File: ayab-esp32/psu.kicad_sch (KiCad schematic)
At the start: 48 parts, among them U401 XL1509, U402 XL1509

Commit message: first draft schematic
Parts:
- removed C? (x4): 10uF, Capacitor_SMD:C_0603_1608Metric, symbol Device:C_Small
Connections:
- net +12V: no longer C?.1, C?.1, C?.1, C?.1, C?.1, C?.1, C?.1, D403.1 (K), J?.1, TP402.1
- net +3V3: no longer C419.2, C421.1, L402.2, R407.2
- net +5V: no longer C418.2, C420.1, L401.2, R406.2
- new net 12V: C?.1, C?.1, C?.1, C?.1, C?.1, C?.1, C?.1, D403.1 (K), J?.1, TP402.1
- new net 3V3: C419.2, C421.1, L402.2, R407.2
- new net 5V: C418.2, C420.1, L401.2, R406.2
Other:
- company: matei repair lab -> matei
- moved on the sheet: C?, D403, J?, TP401, TP402, TP403

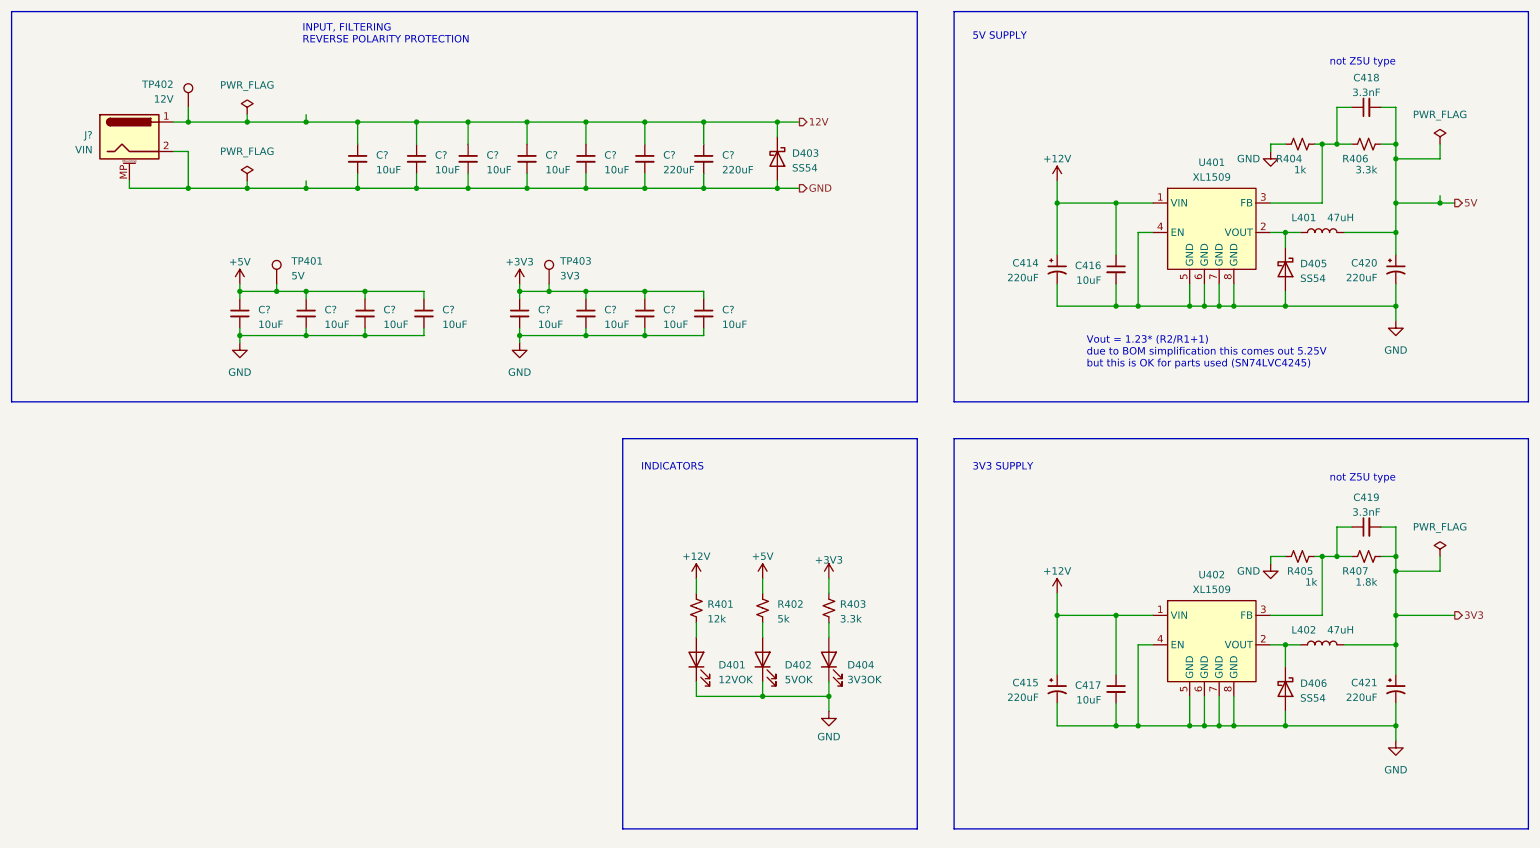
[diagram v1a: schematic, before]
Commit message: add pch MOSFET for polarity protection
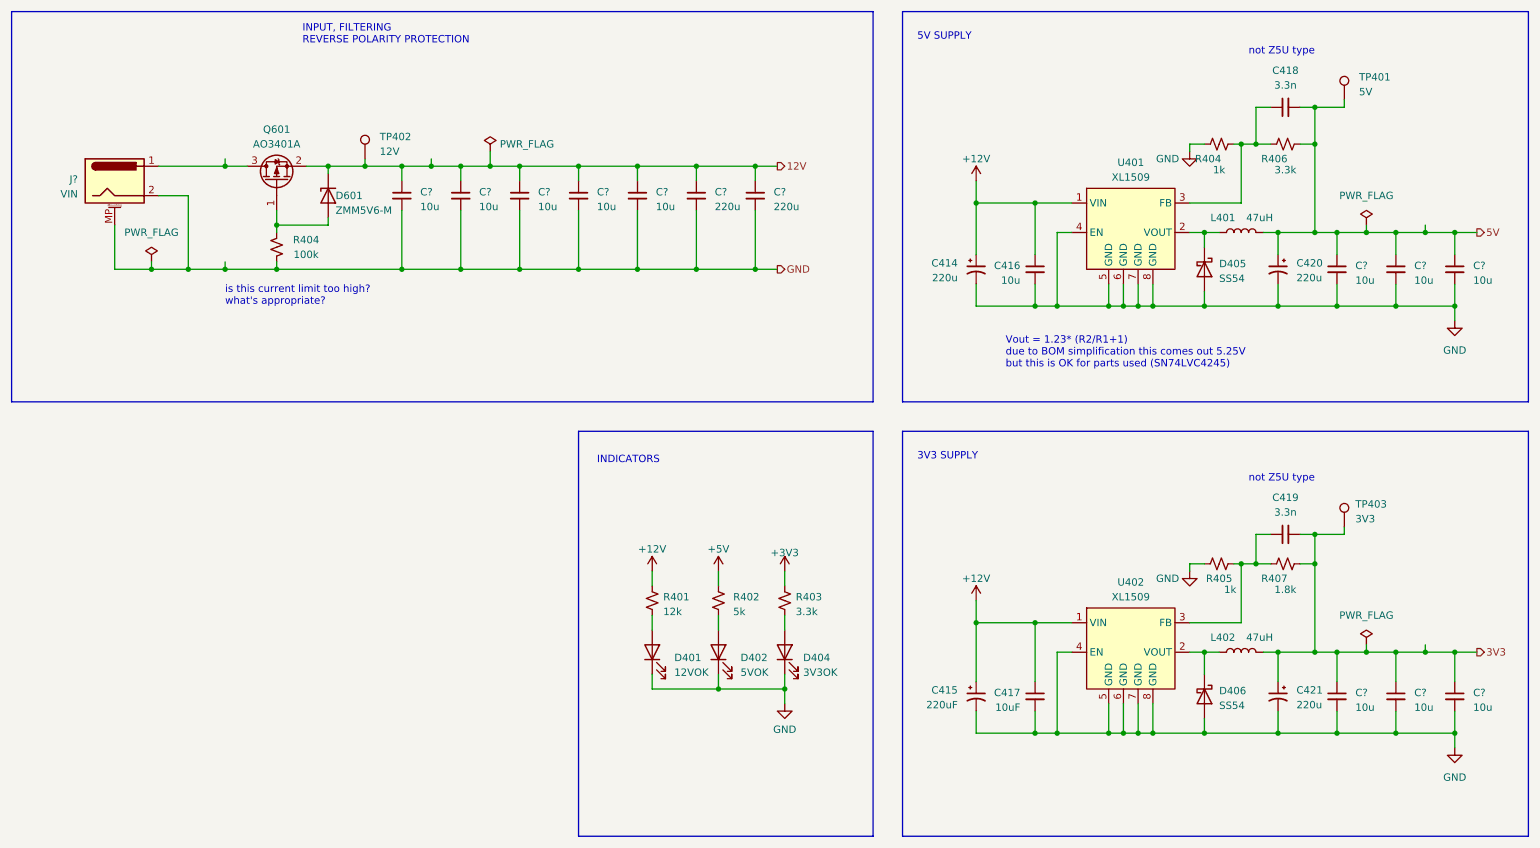
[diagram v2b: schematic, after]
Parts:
- removed C? (x2): 10uF, Capacitor_SMD:C_0603_1608Metric, symbol Device:C_Small
- removed D403: SS54, Diode_SMD:D_SMA, symbol Device:D_Schottky
- added D601: ZMM5V6-M, symbol Device:D_Zener
- added Q601: AO3401A, Package_TO_SOT_SMD:SOT-23, symbol Transistor_FET:AO3401A
- added R404: 100k, Resistor_SMD:R_0603_1608Metric, symbol Device:R_Small_US
- C414, C420, C421, C? (x2): value 220uF -> 220u
- C416, C? (x11): value 10uF -> 10u
- C418, C419: value 3.3nF -> 3.3n
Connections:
- net +3V3: no longer C?.1, C?.1, C?.1, TP403.1
- net +5V: no longer C?.1, C?.1, C?.1, TP401.1
- net 12V: now also D601.1 (K), Q601.2 (S); no longer J?.1
- net 3V3: now also C?.1, C?.1, C?.1, TP403.1
- net 5V: now also C?.1, C?.1, C?.1, TP401.1
- net GND: now also R404.2
- new net: D601.2 (A), Q601.1 (G), R404.1
- new net: J?.1, Q601.3 (D)
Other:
- note added: "is this current limit too high? what's appropriate?"
- moved on the sheet: C414, C415, C416, C417, C418, C419, C420, C421, C?, D401, D402, D404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

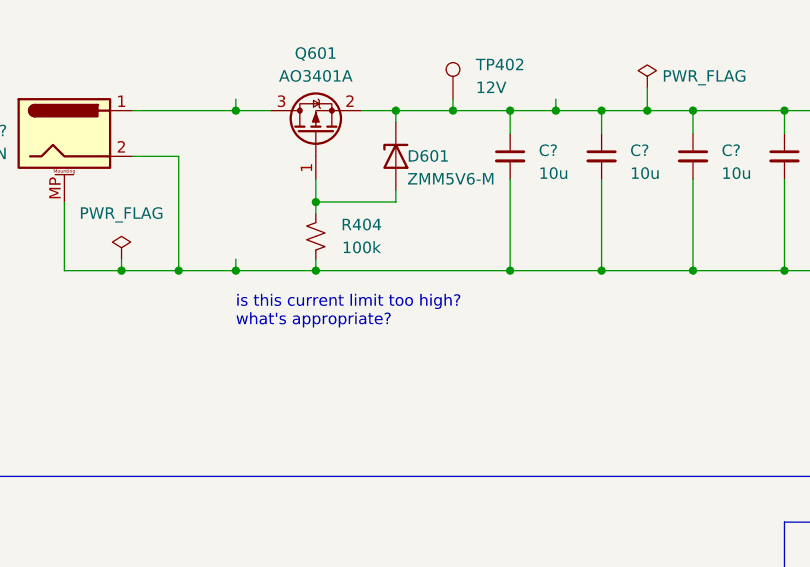
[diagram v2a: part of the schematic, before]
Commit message: update zener current limit resistor
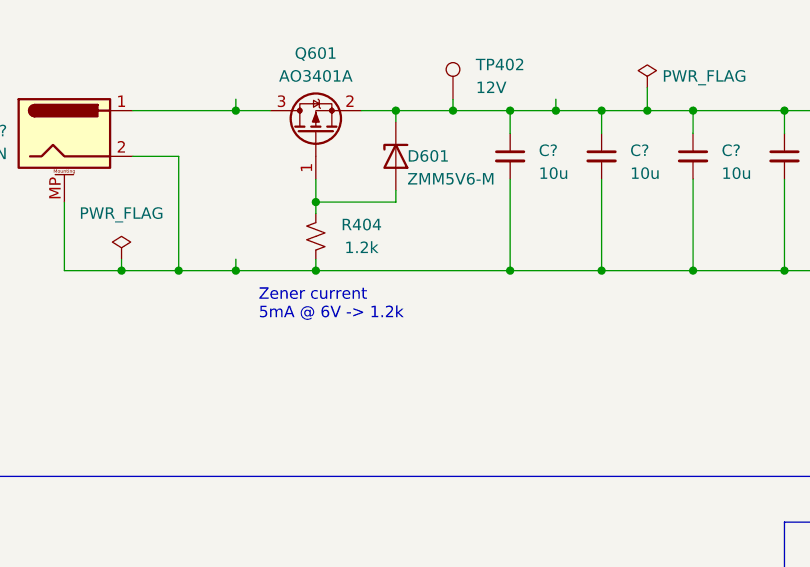
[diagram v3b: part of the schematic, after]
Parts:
- R404: value 100k -> 1.2k
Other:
- note added: "Zener current 5mA @ 6V -> 1.2k"
- note removed: "is this current limit too high? what's appropriate?"
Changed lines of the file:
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@@
     (effects (font (size 1.27 1.27)) (justify left bottom))
   )
-  (text "is this current limit too high?\nwhat's appropriate?"
-    (at 54.61 67.31 0)
+  (text "Zener current \n5mA @ 6V -> 1.2k\n\n" (at 57.15 68.58 0)
     (effects (font (size 1.27 1.27)) (justify left bottom))
   )
@@
       (effects (font (size 1.27 1.27)))
     )
-    (property "Value" "100k" (at 68.58 58.42 0)
-      (effects (font (size 1.27 1.27)))
-    )
+    (property "Value" "1.2k" (at 68.58 58.42 0)
+      (effects (font (size 1.27 1.27)))
+    )

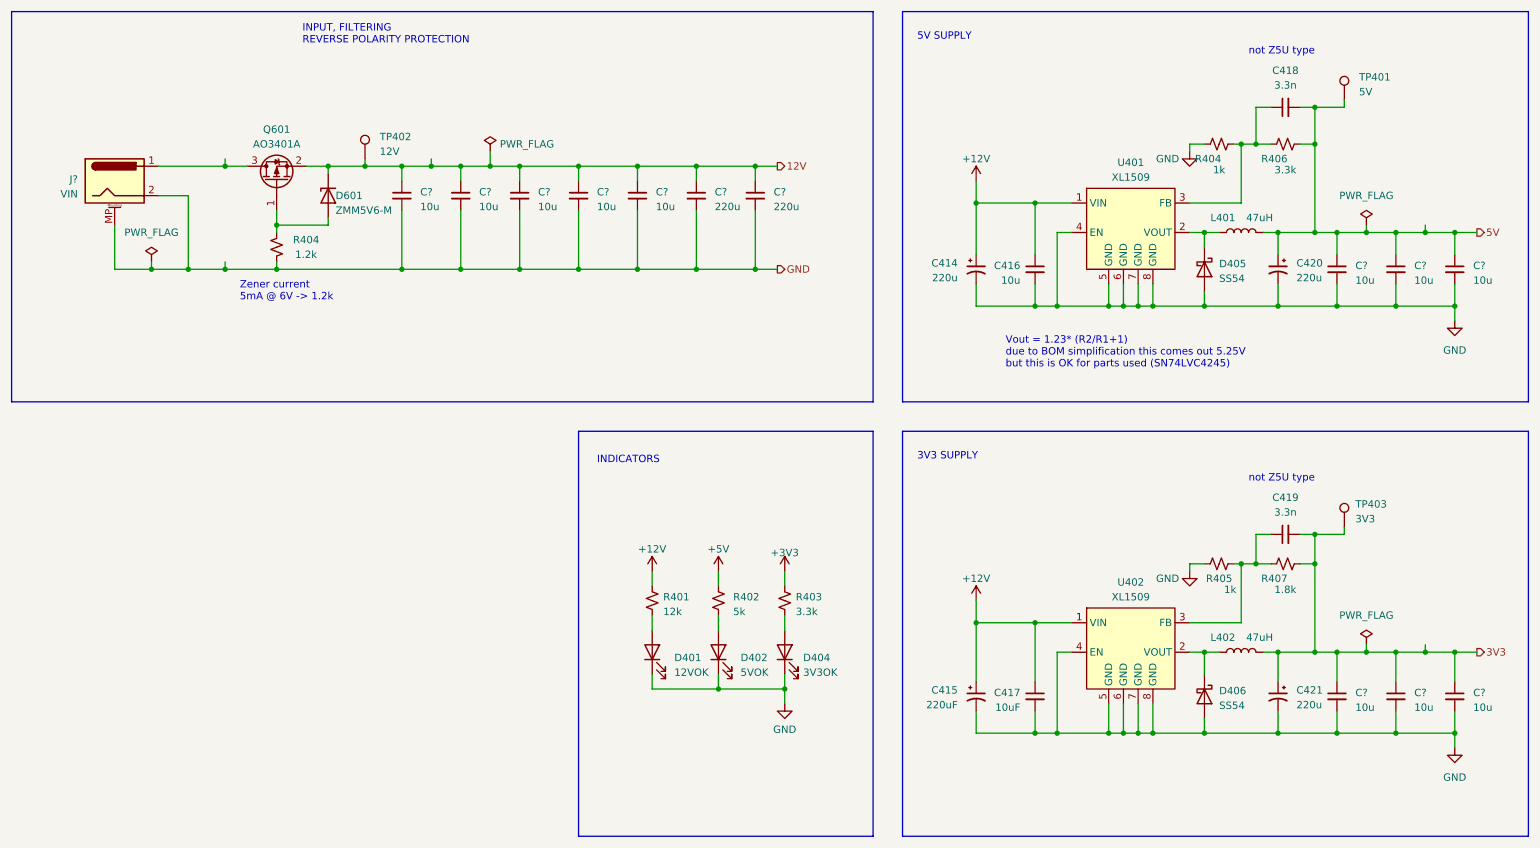
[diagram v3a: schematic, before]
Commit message: add ideal diode, remove extra uln2003a, add comparator for analog EOL sensors
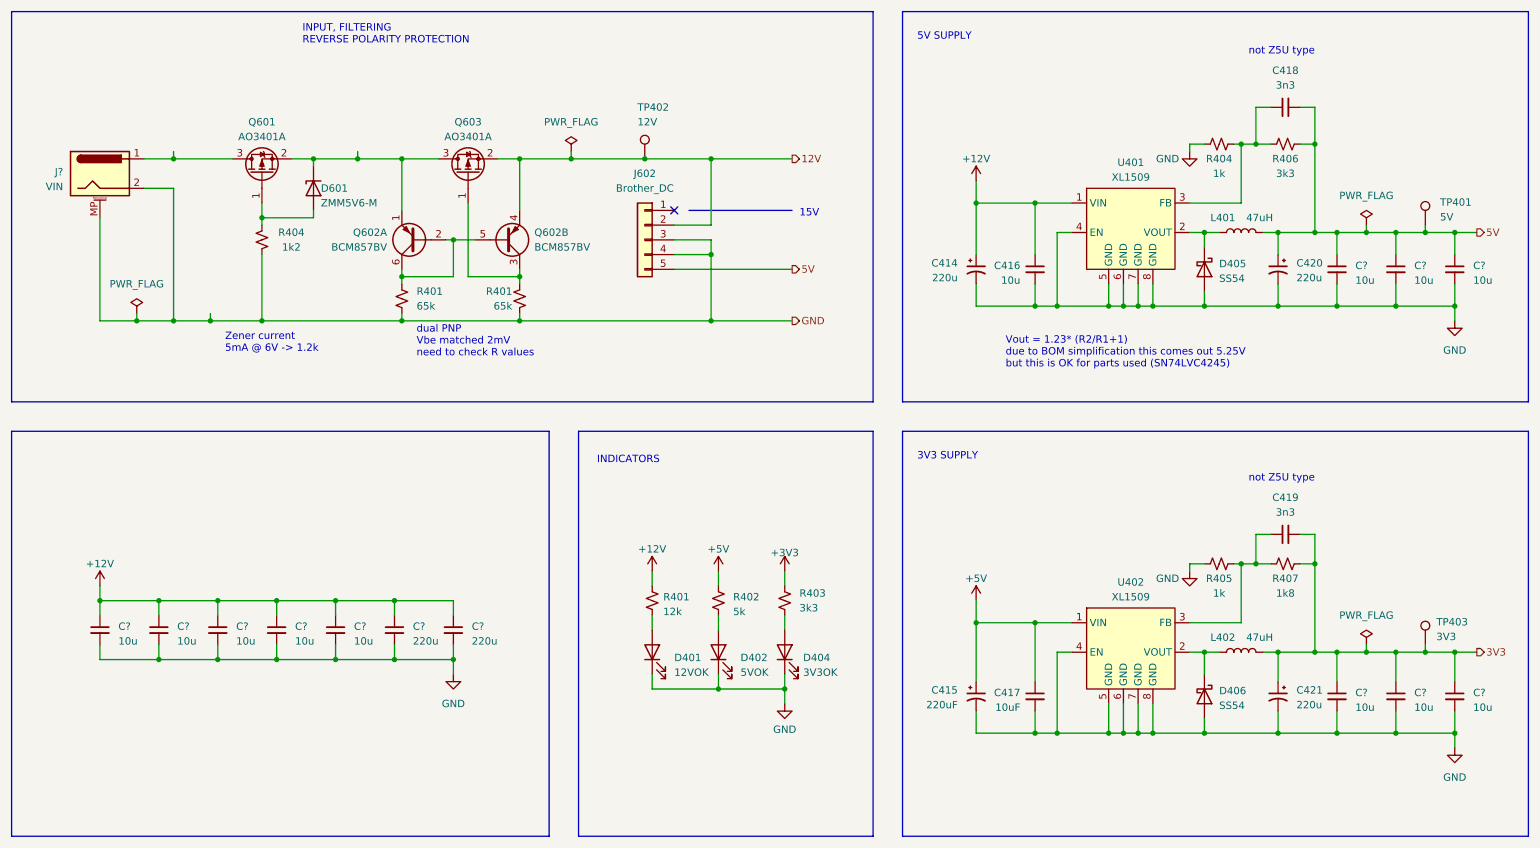
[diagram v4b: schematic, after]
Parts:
- added J602: Brother_DC, symbol Connector_Generic:Conn_01x05
- added Q602: BCM857BV, symbol Device:Q_Dual_PNP_PNP_E1B1C2E2B2C1
- added Q603: AO3401A, Package_TO_SOT_SMD:SOT-23, symbol Transistor_FET:AO3401A
- added R401 (x2): 65k, Resistor_SMD:R_0603_1608Metric, symbol Device:R_Small_US
- C418, C419: value 3.3n -> 3n3
- R403, R406: value 3.3k -> 3k3
- R404: value 1.2k -> 1k2
- R407: value 1.8k -> 1k8
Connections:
- net +12V: now also C?.1, C?.1, C?.1, C?.1, C?.1, C?.1, C?.1; no longer C415.1, C417.1, U402.1 (VIN)
- net +5V: now also C415.1, C417.1, U402.1 (VIN)
- net 12V: now also J602.2 (Pin_2), Q602.4 (E2), Q603.2 (S); no longer C?.1, C?.1, C?.1, C?.1, C?.1, C?.1, C?.1, D601.1 (K), Q601.2 (S)
- net 5V: now also J602.5 (Pin_5)
- net GND: now also J602.3 (Pin_3), J602.4 (Pin_4), R401.2, R401.2
- new net: Q602.3 (C2), Q603.1 (G), R401.1
- new net: D601.1 (K), Q601.2 (S), Q602.1 (E1), Q603.3 (D)
- new net: Q602.2 (B1), Q602.5 (B2), Q602.6 (C1), R401.1
- no-connect marks 0 -> 1
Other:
- note added: "15V"
- note added: "dual PNP Vbe matched 2mV need to check R values"
- moved on the sheet: C?, D601, J?, Q601, R404, TP401, TP402, TP403

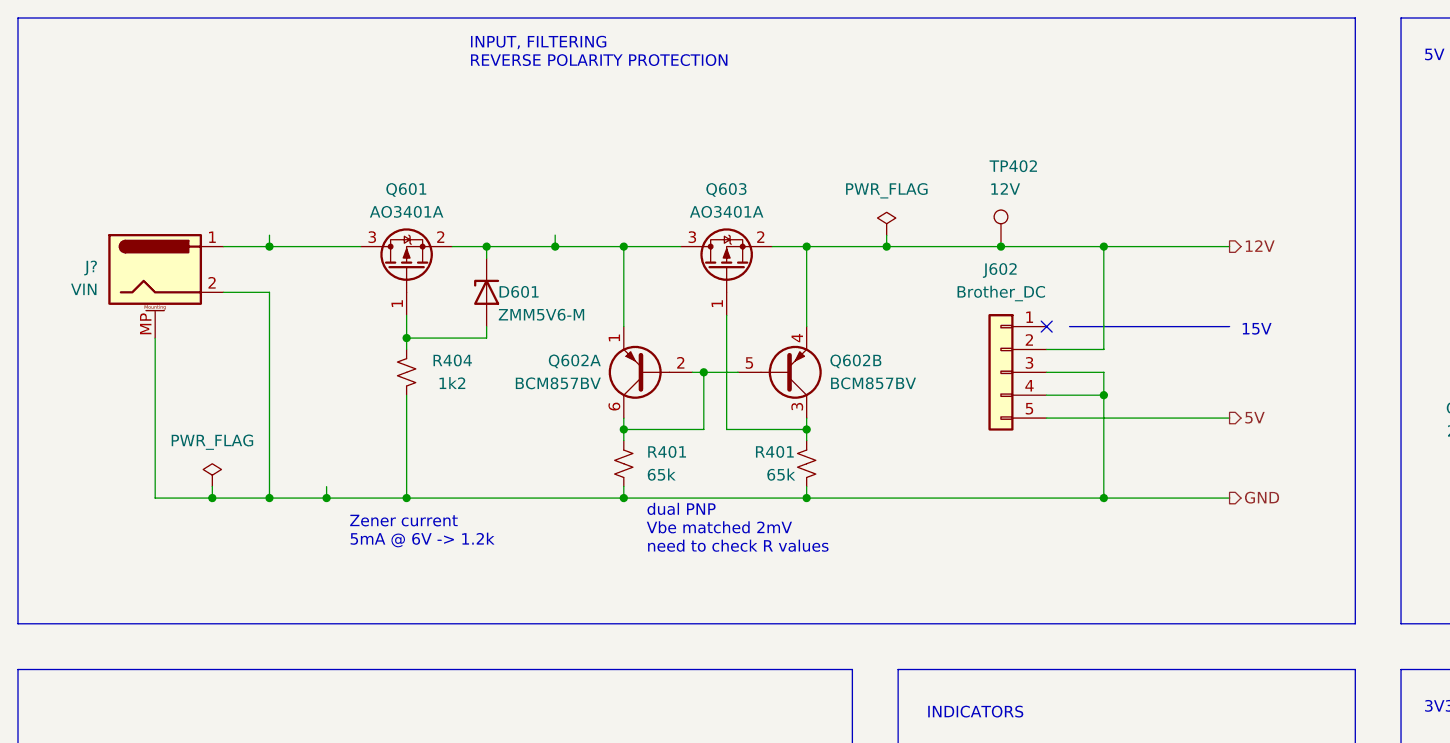
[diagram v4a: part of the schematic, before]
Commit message: fix folder structure and update gitignore
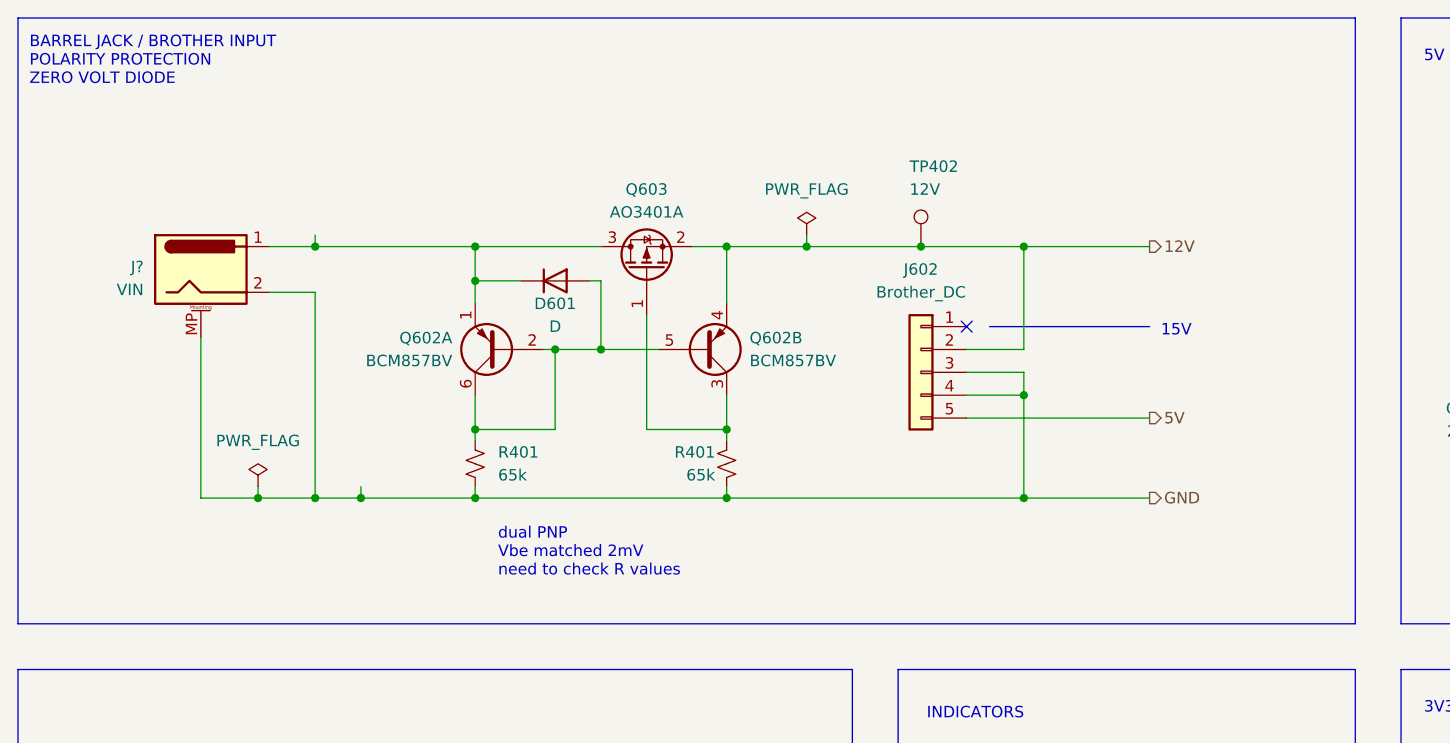
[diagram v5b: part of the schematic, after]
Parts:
- removed D601: ZMM5V6-M, symbol Device:D_Zener
- removed Q601: AO3401A, Package_TO_SOT_SMD:SOT-23, symbol Transistor_FET:AO3401A
- removed R404: 1k2, Resistor_SMD:R_0603_1608Metric, symbol Device:R_Small_US
- added D601: D, symbol ayab-esp32:D
- C414, C415, C420, C421: symbol Device:C_Polarized_Small_US -> ayab-esp32:C_Polarized_Small_US
- C416, C417, C418, C419, C? (x13): symbol Device:C_Small -> ayab-esp32:C_Small
- D401, D402, D404: symbol Device:LED -> ayab-esp32:LED
- D405, D406: symbol Device:D_Schottky -> ayab-esp32:D_Schottky
- J602: symbol Connector_Generic:Conn_01x05 -> ayab-esp32:Conn_01x05
- J?: symbol Connector:Barrel_Jack_MountingPin -> ayab-esp32:Barrel_Jack_MountingPin
- L401, L402: symbol Device:L -> ayab-esp32:L
- Q602: symbol Device:Q_Dual_PNP_PNP_E1B1C2E2B2C1 -> ayab-esp32:Q_Dual_PNP_PNP_E1B1C2E2B2C1
- Q603: symbol Transistor_FET:AO3401A -> ayab-esp32:AO3401A
- R401, R402, R403, R404, R405, R406, R407: symbol Device:R_Small_US -> ayab-esp32:R_Small_US
- TP401, TP402, TP403: symbol Connector:TestPoint -> ayab-esp32:TestPoint
- U401, U402: symbol matei:XL1509 -> ayab-esp32:XL1509
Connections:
- net at Q602.1 (E1), Q603.3 (D): now also J?.1, D601.1 (K)
- net at Q602.2 (B1), Q602.5 (B2), Q602.6 (C1)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: now also D601.2 (A)
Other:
- note added: "BARREL JACK / BROTHER INPUT POLARITY PROTECTION ZERO VOLT DIODE"
- note removed: "INPUT, FILTERING REVERSE POLARITY PROTECTION"
- note removed: "Zener current 5mA @ 6V -> 1.2k"
- moved on the sheet: J602, J?, Q602A, Q602B, Q603, R401, TP402
